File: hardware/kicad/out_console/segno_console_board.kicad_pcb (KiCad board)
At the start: 2 copper layers, 115 x 96 mm, 58 parts, among them J1 RaspberryPi_Pico_SMD_HandSold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, J10 JST_XH_B2B-XH-A_1x02_P2.50mm_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, J11 JST_XH_B2B-XH-A_1x02_P2.50mm_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, J12 JST_XH_B2B-XH-A_1x02_P2.50mm_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, J13 JST_XH_B2B-XH-A_1x02_P2.50mm_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, J14 JST_XH_B2B-XH-A_1x02_P2.50mm_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, J15 JST_XH_B2B-XH-A_1x02_P2.50mm_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, J16 JST_XH_B2B-XH-A_1x02_P2.50mm_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, J17 JST_XH_B2B-XH-A_1x02_P2.50mm_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, J18 JST_XH_B2B-XH-A_1x02_P2.50mm_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, J19 JST_XH_B2B-XH-A_1x02_P2.50mm_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, J2 IDC-Header_2x20_P2.54mm_Verti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, J20 JST_XH_B3B-XH-A_1x03_P2.50mm_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, J21 JST_XH_B3B-XH-A_1x03_P2.50mm_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, J22 PinHeader_2x04_P2.54mm_Vertic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, J3 JST_XH_B4B-XH-A_1x04_P2.50mm_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, J4 JST_XH_B3B-XH-A_1x03_P2.50mm_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, J5 JST_XH_B2B-XH-A_1x02_P2.50mm_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, J6 JST_XH_B8B-XH-A_1x08_P2.50mm_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, J7 JST_XH_B3B-XH-A_1x03_P2.50mm_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, J8 JST_XH_B2B-XH-A_1x02_P2.50mm_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, J9 JST_XH_B2B-XH-A_1x02_P2.50mm_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, U1 DIP-14_W7.62mm, U2 DIP-6_W7.62mm

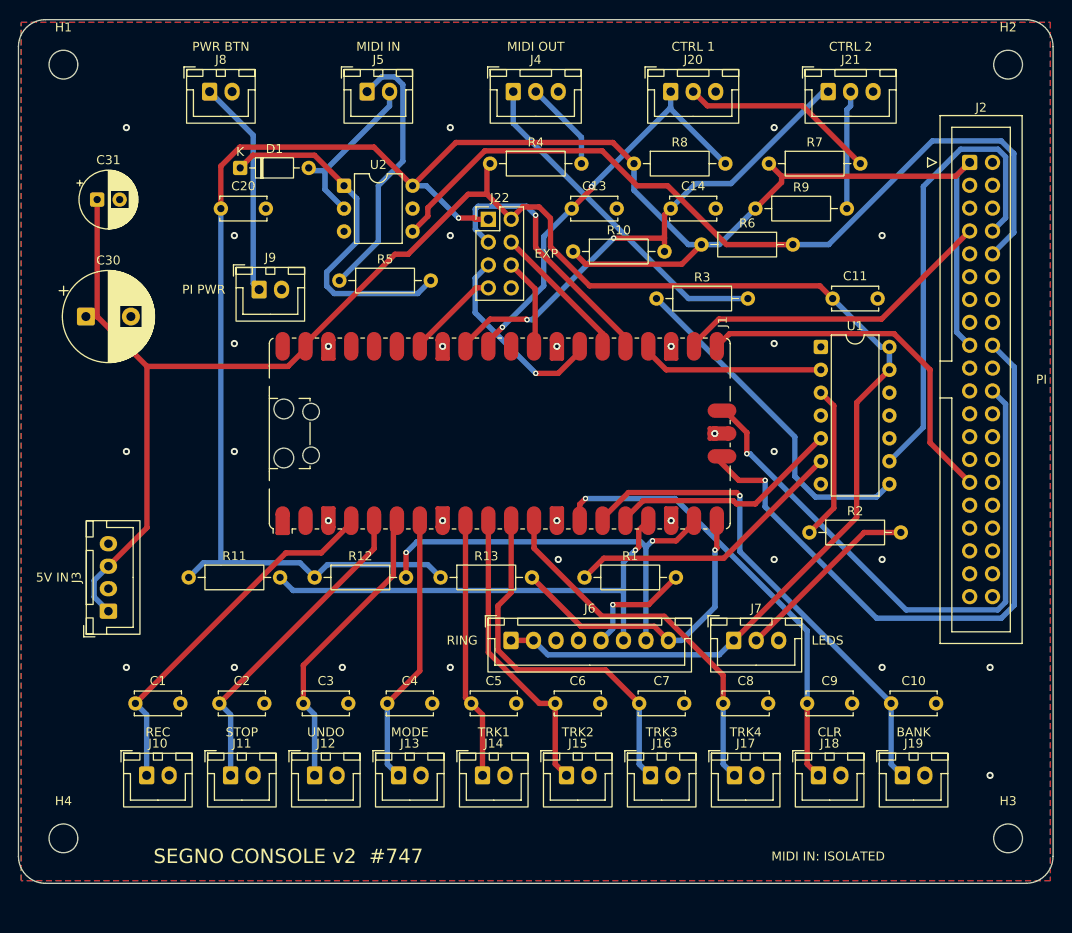
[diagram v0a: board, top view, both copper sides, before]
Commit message: fix(hardware): disc caps to 2.5 mm lead pitch
The 16 discs sat on a 5.00 mm land. Commodity '104' parts ship on 2.5 mm spacing,
so that land meant splaying every lead or sourcing an unusual part. Changing the
board is cheaper than changing the BOM.

C30 deliberately keeps its 10 mm / 5 mm land: order a 470uF at 25 V or 35 V, as
the common 16 V part is 8 x 11.5 mm on 3.5 mm pitch and will not fit.

Refs #747
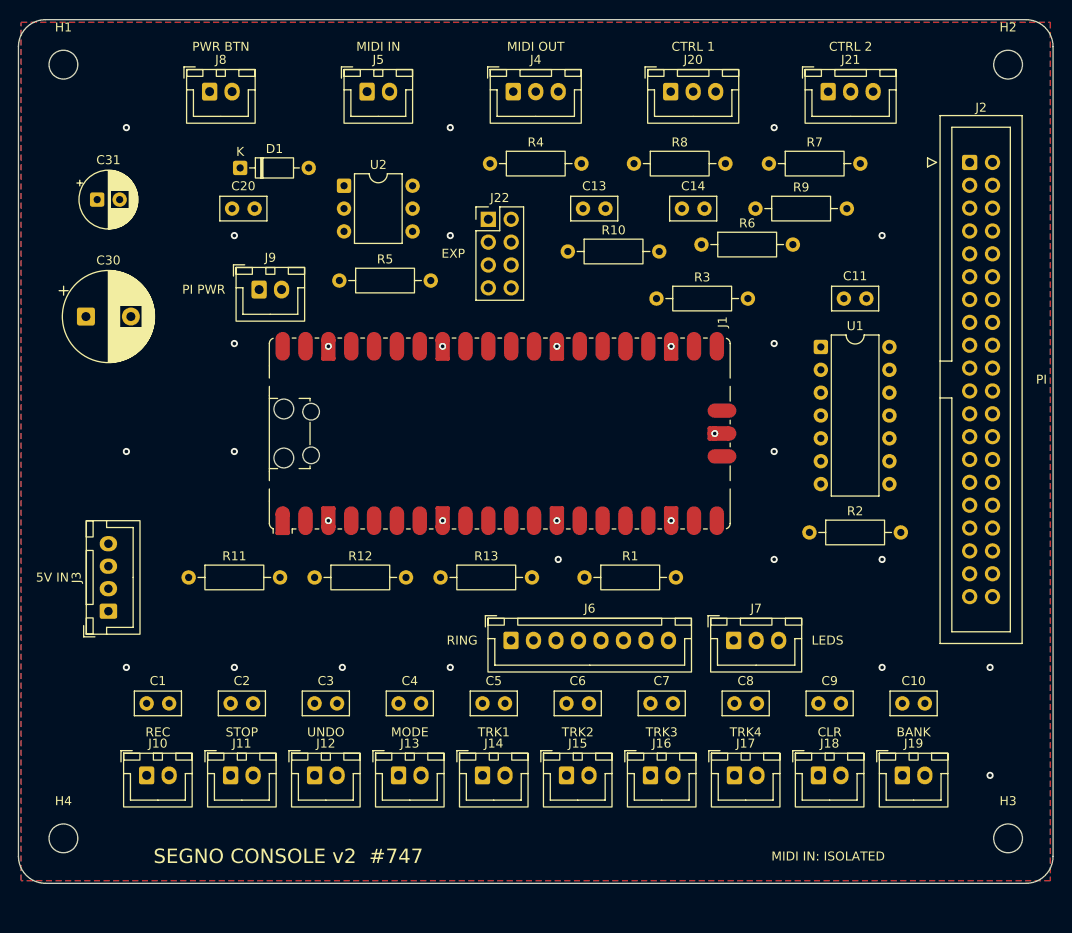
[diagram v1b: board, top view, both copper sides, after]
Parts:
- C1, C10, C11, C13, C14, C2, C20, C3, C4, C5, C6, C7, C8, C9: value C_Disc_D5.0mm_W2.5mm_P5.00mm -> C_Disc_D5.0mm_W2.5mm_P2.50mm; footprint C_Disc_D5.0mm_W2.5mm_P5.00mm -> C_Disc_D5.0mm_W2.5mm_P2.50mm
- moved C2 1.25 mm to (123.6, 136.0)
- moved C5 1.25 mm to (151.6, 136.0)
- moved C8 1.25 mm to (179.6, 136.0)
- moved C1 1.25 mm to (114.2, 136.0)
- moved C10 1.25 mm to (198.2, 136.0)
- moved C11 1.25 mm to (191.8, 91.0)
- moved C13 1.25 mm to (162.8, 81.0)
- moved C14 1.25 mm to (173.8, 81.0)
- moved C20 1.25 mm to (123.8, 81.0)
- moved C4 1.25 mm to (142.2, 136.0)
- moved C7 1.25 mm to (170.2, 136.0)
- moved C3 1.25 mm to (132.9, 136.0)
- moved C6 1.25 mm to (160.9, 136.0)
- moved C9 1.25 mm to (188.9, 136.0)
- moved R10 0.58 mm to (161.1, 85.8)
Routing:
- net +5V: track 222.6 -> 0.00 mm
- net +3V3: track 222.4 -> 0.00 mm, vias 1 -> 0
- net MIDI_RX: track 92.9 -> 0.00 mm
- net SWCLK: track 73.0 -> 0.00 mm, vias 1 -> 0
- net SWDIO: track 67.3 -> 0.00 mm, vias 1 -> 0
- net SW_BANK: track 55.4 -> 0.00 mm, vias 1 -> 0
- net CTRL2_TIP: track 55.3 -> 0.00 mm, vias 2 -> 0
- net ENC_A: track 53.2 -> 0.00 mm, vias 1 -> 0
- net MIDI_TX: track 52.2 -> 0.00 mm
- net SW_CLEAR: track 50.0 -> 0.00 mm, vias 1 -> 0
- net ENC_B: track 47.2 -> 0.00 mm, vias 2 -> 0
- net CTRL1_TIP: track 45.4 -> 0.00 mm, vias 2 -> 0
- net SW_TRACK3: track 41.7 -> 0.00 mm
- net SW_TRACK4: track 41.6 -> 0.00 mm
- net SW_RECPLAY: track 41.1 -> 0.00 mm
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
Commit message: fix(hardware): the console board comes back DRC-clean
133 violations to 0, with 0 unconnected, on three consecutive routing runs
that each found a different solution -- so it is the board that is clean,
not one lucky roll of the autorouter.

102 holes_co_located: every one was a stitching via sitting dead on the
centre of a plated through-hole pad, put there by _stitch_gnd(), which
dropped a via on every GND pad without asking what kind of pad it was. A
plated hole already joins both layers, so those vias connected nothing and
only asked CAM to drill the same coordinate twice. Vias now go BESIDE the
pad -- offset toward the part's own body, since a pad's fan-out leaves
outward and a via in that lane cost SW_TRACK3 its route -- with a stub
back to the pad, and a keepout list of every pad on the board that the
blind lattice is also checked against.

31 via_dangling: lattice vias left in pour islands the fill deleted. That
cannot be known at placement time, because the fill happens after routing,
so it is no longer guessed: --prune-vias pours, asks DRC which vias are
dangling, deletes exactly those, and repeats until a pour comes back with
none. route_console_board.sh runs it after the SES import.

14 silk_overlap: the pinned label rows never entered the occupancy list,
so all ten footswitch designators were placed 0.07 mm from their own
labels. Labels are now measured as rendered rather than estimated from
character counts, and the gate checks silk against silk as well.

Two starved_thermal at J6 were the same problem as the dangling vias seen
from the other end: the lattice cannot place a via near a connector, so
the pour fragments exactly where the headers are. Tying every GND pad
fixes both; an 8 mm lattice was tried first and is the wrong lever, since
it does not reach the connectors either and its extra obstacles in the
open middle left SWCLK unrouted.

Gates that could not fail, found by the same audit:

- THERMALS ran before the pours existed, so it looped over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
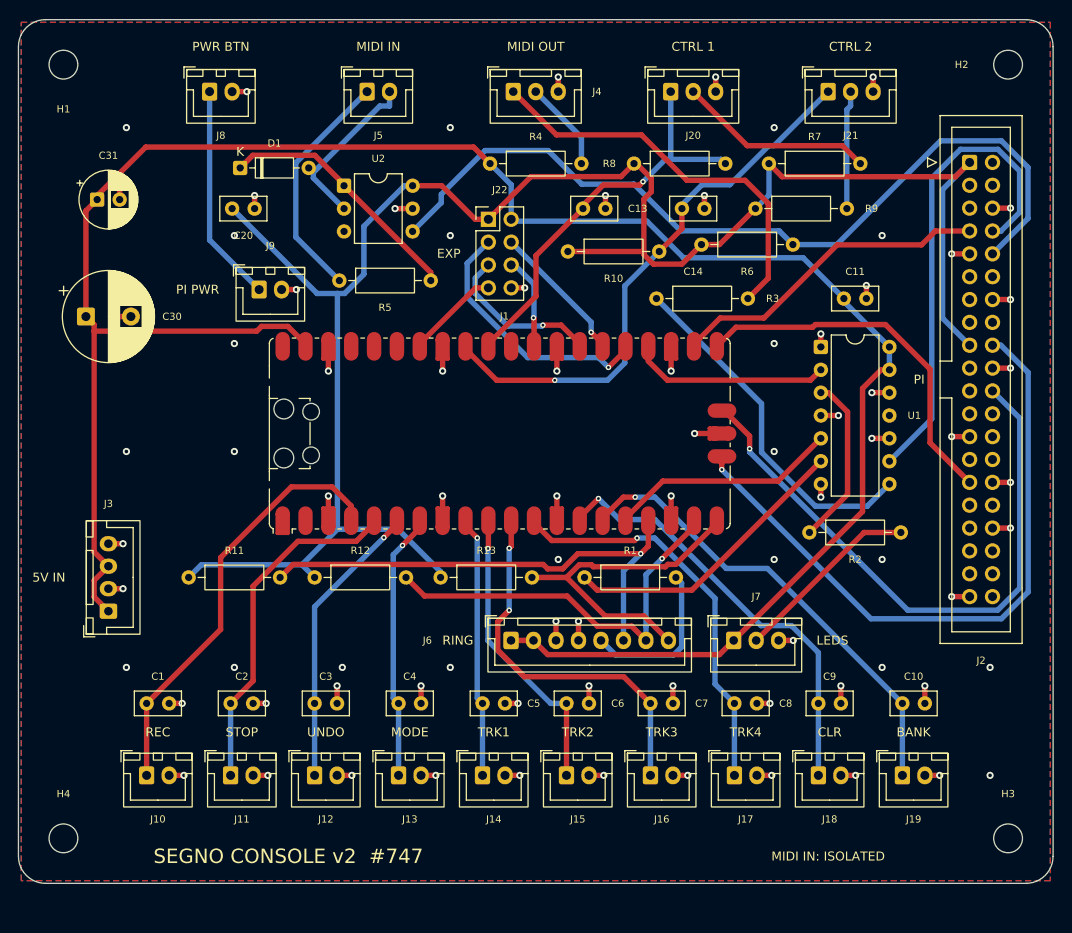
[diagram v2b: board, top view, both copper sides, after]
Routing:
- net +5V: track 0.00 -> 242.2 mm
- net +3V3: track 0.00 -> 209.1 mm
- net GND: track 0.00 -> 113.1 mm
- net MIDI_RX: track 0.00 -> 94.2 mm
- net SWCLK: track 0.00 -> 73.6 mm, vias 0 -> 1
- net SWDIO: track 0.00 -> 68.3 mm, vias 0 -> 1
- net CTRL2_TIP: track 0.00 -> 61.9 mm, vias 0 -> 1
- net ENC_A: track 0.00 -> 56.0 mm, vias 0 -> 1
- net MIDI_TX: track 0.00 -> 54.0 mm
- net SW_BANK: track 0.00 -> 52.1 mm, vias 0 -> 1
- net SW_CLEAR: track 0.00 -> 48.5 mm, vias 0 -> 1
- net SW_RECPLAY: track 0.00 -> 47.9 mm
- net CTRL1_TIP: track 0.00 -> 45.7 mm, vias 0 -> 1
- net ENC_B: track 0.00 -> 45.1 mm, vias 0 -> 1
- net N$1: track 0.00 -> 45.0 mm
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
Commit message: fix(hardware): the console board fits the 100 x 100 mm fab tier
99.5 mm square, down from 115 x 96. Every prototype fab prices 2-layer boards
in a cheap tier that stops at 100 x 100, and the old width was over it for no
structural reason: the enclosure bay is 342 x 193, so nothing mechanical
wanted those 15 mm. 99.5 rather than 100.0 because Edge.Cuts is a 0.1 mm line
and a 100.0 outline measures 100.1 across the outside of it -- the half
millimetre costs nothing and means no CAM operator has to make that call.

Still 0 DRC violations and 0 unconnected, and the ratsnest went DOWN, from
1573 mm to 1473: a smaller board shortens every fan-out.

The width is now set by one thing, and it is worth knowing which: the ten
footswitch JSTs are 92.2 mm of outline at their pitch floor, so the board
cannot go below ~93 mm without giving up one connector per pedal. Everything
else fits inside that -- the widest other row is J3 + module + U1 + ribbon at
80.5 mm.

What the squeeze cost, and what it bought:

- U1 no longer fits between the module and the ribbon's column, so the module
  is pinned from the right at x 43. SW_BANK pays for it: 40.7 mm of the 42 mm
  hop limit, the tightest number on the board. The limit stays where it is
  rather than being relaxed to fit -- the next mm has to come from the
  floorplan, not the gate. The ratsnest budget is re-derived at 1610 mm.
- R2 stands upright in the 8 mm channel beside the module; a 12.3 mm axial
  cannot lie flat there and there is nowhere else for it.
- R5, R10 and D1 are hand-placed: the band is shoulder to shoulder and the
  spiral cannot find 12.3 mm of axial in range. D1 was the interesting one --
  it clamps the opto's LED, so it belongs in the isolated pocket with U2, R5
  and J5, but the spiral had parked it 15 mm away, straight across the only
  lane from J8 to J9, and PWR_BTN would not route at all. The isolation gate
  could not object: D1 shares the DIN-side nets, so it is exempt by
  construction.
- The designator 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
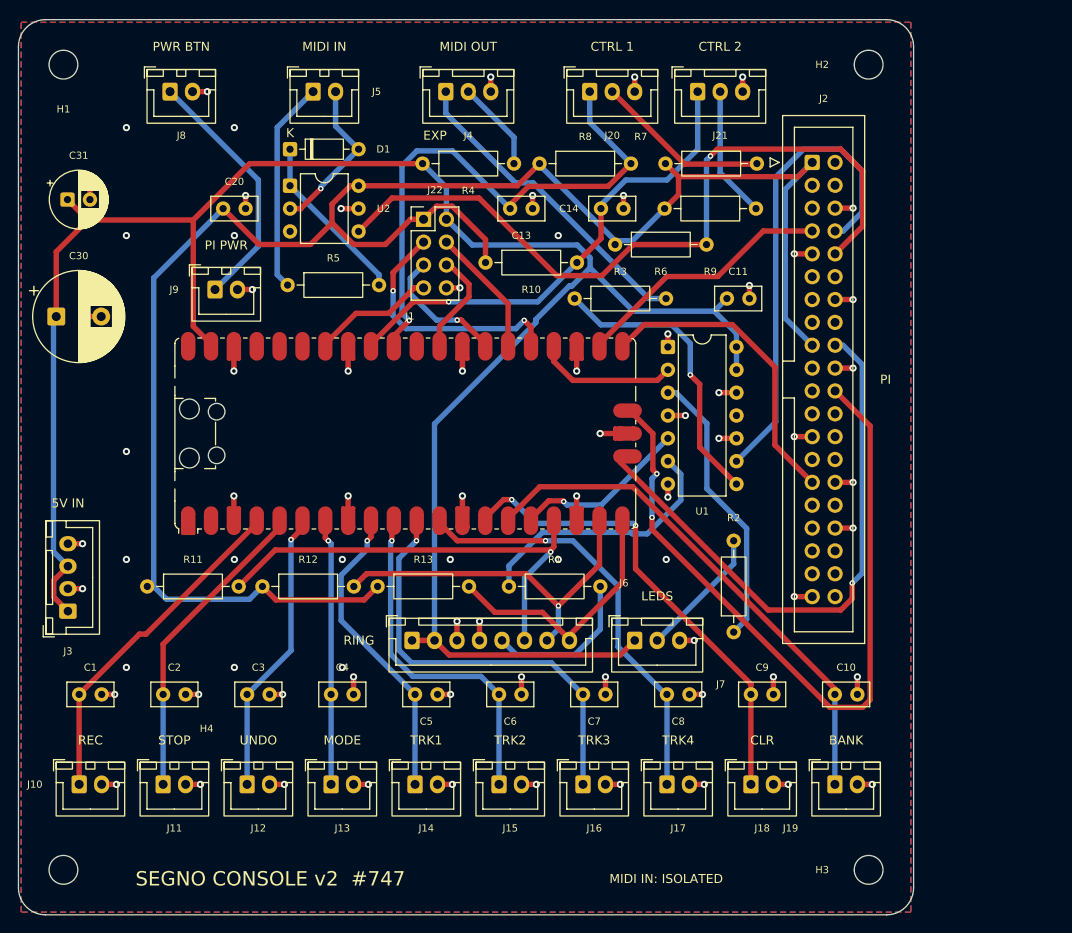
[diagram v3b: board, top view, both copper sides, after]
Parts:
- moved J2 17.5 mm to (188.2, 75.9)
- moved U1 17.0 mm to (172.2, 96.4)
- moved H3 15.9 mm to (194.5, 154.5)
- moved H2 15.5 mm to (194.5, 65.0)
- moved J21 14.5 mm to (175.5, 68.0)
- moved R2 13.9 mm to (179.5, 128.1), turned to 90 degrees
- moved C11 13.0 mm to (178.8, 91.0)
- moved R7 11.5 mm to (171.9, 76.0)
- moved J6 11.0 mm to (143.8, 129.0)
- moved J7 11.0 mm to (168.5, 129.0)
- moved J1 10.5 mm to (143.0, 106.0)
- moved R8 10.5 mm to (157.9, 76.0)
- moved R9 10.1 mm to (171.8, 81.0)
- moved R6 9.60 mm to (166.3, 85.0)
- moved R10 9.23 mm to (151.9, 87.0)
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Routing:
- net CTRL1_TIP: track 45.7 -> 62.1 mm
- net SWDIO: track 68.3 -> 84.5 mm, vias 1 -> 2
- net IND_DATA_BUF: track 19.0 -> 31.4 mm
- net +5V: track 242.2 -> 231.2 mm
- net MIDI_RX: track 94.2 -> 83.9 mm, vias 0 -> 1
- net SW_RECPLAY: track 47.9 -> 37.9 mm
- net N$1: track 45.0 -> 35.4 mm
- net SWCLK: track 73.6 -> 64.2 mm
- net N$4: track 28.1 -> 19.2 mm
- net ENC_SW: track 37.7 -> 29.2 mm
- net CTRL2_TIP: track 61.9 -> 54.1 mm
- net LINK_RX: track 36.1 -> 29.1 mm
- net MIDI_OUT_BUF: track 39.6 -> 32.7 mm, vias 0 -> 1
- net LINK_TX: track 41.2 -> 34.4 mm
- net IND_DATA: track 22.2 -> 15.7 mm
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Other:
- board size 115 x 96 mm -> 99.5 x 99.5 mm

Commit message: feat(hardware): bond the console board to the chassis, deliberately
The four mounting holes were bare NPTH -- no copper -- so the board floated
inside an earthed metal box. That was never a decision; it was the default
footprint. And it did not float in practice: the rear panel carries two USB 3.0
couplers, two DIN-5 sockets and two D-series TRS jacks, all bolted through
metal, and the TRS sleeves ARE this board's GND. A floating board in a box full
of bonded connector flanges is the worst case -- the loops exist anyway, through
long, undefined, high-impedance paths.

So: ONE hard DC bond, at H1. Top-left, the corner nearest where the outside
world arrives -- power button, MIDI, CTRL and ten footswitch leads all land
along the top edge -- and diagonally away from the ribbon, so an ESD strike on a
pedal cable reaches the case instead of travelling the 40-way into the Pi.

H2/H3/H4 get the option instead of the bond: an isolated pad with a 10 nF 2 kV
cap and a 1 M bleeder to GND, both DNF. A second DC bond would close a
mains-frequency loop (chassis -> Pi -> ribbon -> here -> chassis), which is where
hum comes from; a capacitor will not. 10 nF is ~318 k at 50 Hz, so no hum current
can flow, and ~0.16 ohm at 100 MHz, so ESD and RF still get a short path into the
case. The board ships single-point bonded and the pads exist so EMC testing can
change that with an iron rather than a respin.

H1..H4 are now REAL PARTS IN THE NETLIST rather than footprints the layout script
synthesised. One of them carries GND, and a chassis bond is a connection, so it
belongs in the source of truth. `_mounting_holes()` is deleted.

CHASSIS_BOND gates it: exactly one hole hard-bonded to GND -- two close the loop,
zero leaves the board floating -- and every other hole reaching ground only
through a capacitor AND a bleeder, never bare copper. Two negative controls, one
per half. The netlist self-test is now 12 controls, the layout one 8, all biting
the gate they name.

Layout fallout, all meas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
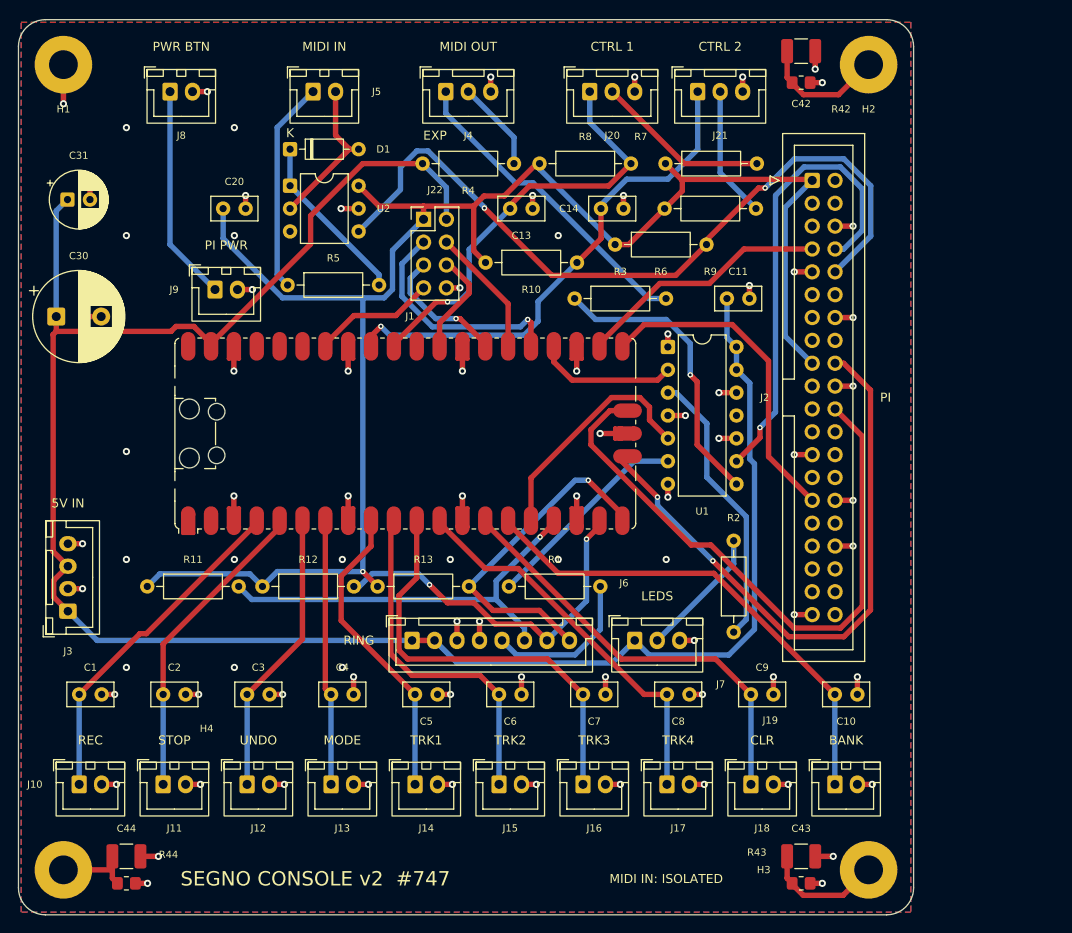
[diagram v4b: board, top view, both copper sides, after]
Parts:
- added C42: C_1210_3225Metric_Pad1.33x2.70mm_HandSolder, C_1210_3225Metric_Pad1.33x2.70mm_HandSolder, F.Cu at (187.0, 63.5)
- added C43: C_1210_3225Metric_Pad1.33x2.70mm_HandSolder, C_1210_3225Metric_Pad1.33x2.70mm_HandSolder, F.Cu at (187.0, 153.0)
- added C44: C_1210_3225Metric_Pad1.33x2.70mm_HandSolder, C_1210_3225Metric_Pad1.33x2.70mm_HandSolder, F.Cu at (112.0, 153.0)
- added R42: R_0805_2012Metric_Pad1.20x1.40mm_HandSolder, R_0805_2012Metric_Pad1.20x1.40mm_HandSolder, F.Cu at (187.0, 67.0)
- added R43: R_0805_2012Metric_Pad1.20x1.40mm_HandSolder, R_0805_2012Metric_Pad1.20x1.40mm_HandSolder, F.Cu at (187.0, 156.0)
- added R44: R_0805_2012Metric_Pad1.20x1.40mm_HandSolder, R_0805_2012Metric_Pad1.20x1.40mm_HandSolder, F.Cu at (112.0, 156.0)
- H1, H2, H3, H4: value MountingHole_3.2mm_M3 -> MountingHole_3.2mm_M3_Pad; footprint MountingHole_3.2mm_M3 -> MountingHole_3.2mm_M3_Pad
- moved J2 2.00 mm to (188.2, 77.9)
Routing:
- net SWDIO: track 84.5 -> 68.6 mm, vias 2 -> 0
- net +3V3: track 202.9 -> 187.9 mm, vias 0 -> 1
- net GND: track 112.6 -> 127.0 mm, vias 75 -> 82
- net CTRL1_TIP: track 62.1 -> 47.7 mm
- net CHASSIS_H2: track 0.00 -> 14.2 mm
- net CHASSIS_H3: track 0.00 -> 13.5 mm
- net CHASSIS_H4: track 0.00 -> 8.67 mm
- net ENC_SW: track 29.2 -> 37.9 mm, vias 0 -> 1
- net RING_DATA: track 19.5 -> 26.4 mm, vias 1 -> 0
- net RING_DATA_BUF: track 29.5 -> 23.4 mm
- net SW_CLEAR: track 53.1 -> 47.7 mm, vias 2 -> 0
- net ENC_A: track 51.0 -> 46.6 mm
- net PWR_BTN: track 28.1 -> 24.1 mm
- net SW_TRACK4: track 47.4 -> 43.4 mm, vias 1 -> 0
- net +5V: track 231.2 -> 227.5 mm
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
